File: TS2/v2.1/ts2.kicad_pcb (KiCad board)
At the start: 2 copper layers, 134.6 x 208.3 mm, 110 parts, among them P1 FTDI (TERMINAL), P2 FTDI (HOST), P3 +5V POWER, SW1 RESET, SW2 SINGLE STEP/RUN, SW3 STEP, SW4 ABORT, SW5 POWER, U1 555, U10 74LS32, U11 HM6264, U12 28C64, U13 HM6264, U14 28C64, U15 HM6264, U16 28C64, U17 HM6264, U18 28C64, U19 74LS20, U2 8 MHz, U20 74LS74, U21 74LS161, U22 74LS161, U23 74LS74, U24 74LS260, U25 74LS260, U26 74LS138, U27 74LS138, U28 74LS148, U29 6850, U3 74LS00, U30 6850, U31 74HC4060, U32 74LS138, U33 74LS138, U34 74LS00, U35 74LS74, U36 74LS27, U37 74LS00, U4 74LS06, U5 74LS04, U6 68000, U7 74LS08, U8 74LS32, U9 74LS32, Y1 2.4576MHz

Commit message: Rev 2.1.1 changes.
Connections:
- P3 pad 2: Net-(P3-Pad2) -> POWER
- SW5 pad 1: Net-(P3-Pad2) -> POWER
- U29 pad 1: (no net) -> GND
- U29 pad 12: (no net) -> VCC
- U30 pad 1: (no net) -> GND
- U30 pad 12: (no net) -> VCC
- U6 pad 7: LDS* -> UDS*
- U6 pad 8: UDS* -> LDS*
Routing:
- net UDS*: track 265.0 -> 561.0 mm, vias 5 -> 9
- net POWER: track 38.1 -> 277.3 mm, vias 0 -> 1
- net Net-(P3-Pad2): track 202.7 -> 0.00 mm
- net LDS*: track 274.4 -> 224.2 mm, vias 5 -> 6
- net VCC: track 1108.4 -> 1139.0 mm, vias 1 -> 2
- net GND: track 1388.1 -> 1408.3 mm, vias 1 -> 2
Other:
- board text added: "TS2 Single Board Computer Rev 2.1.1 Copyright (c) 2017 Jeff Tranter <tranter@pobox.com>"
- board text removed: "TS2 Single Board Computer Rev 2.1 Copyright (c) 2017 Jeff Tranter <tranter@pobox.com>"

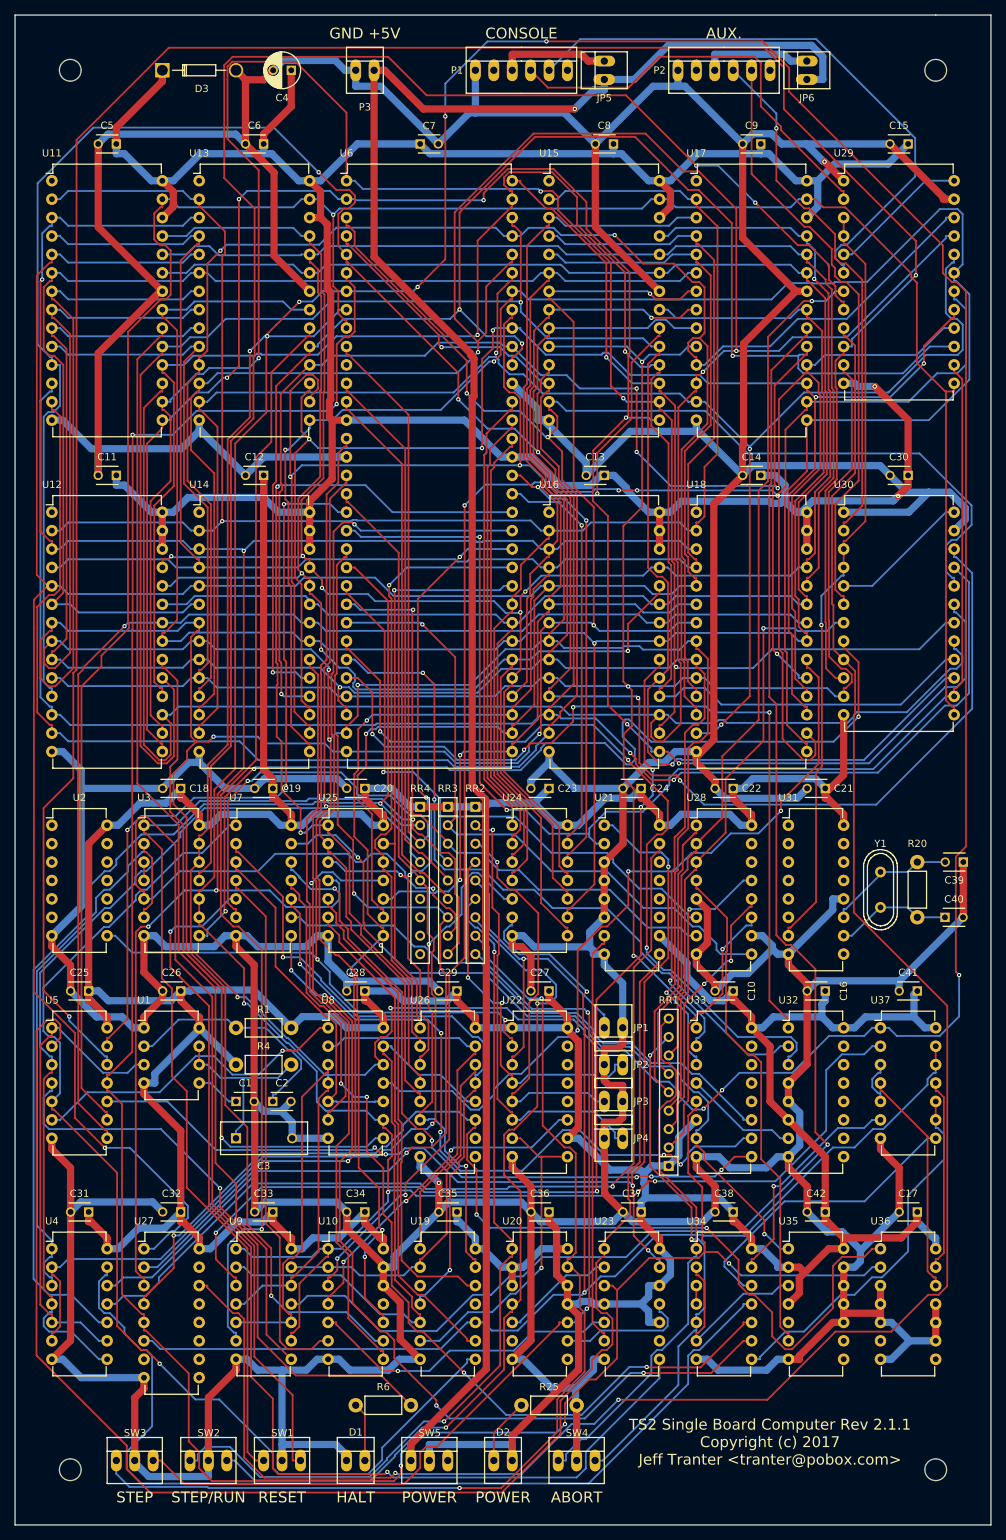
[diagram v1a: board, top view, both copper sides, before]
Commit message: Check in rev 2.1.1 PCB layout.
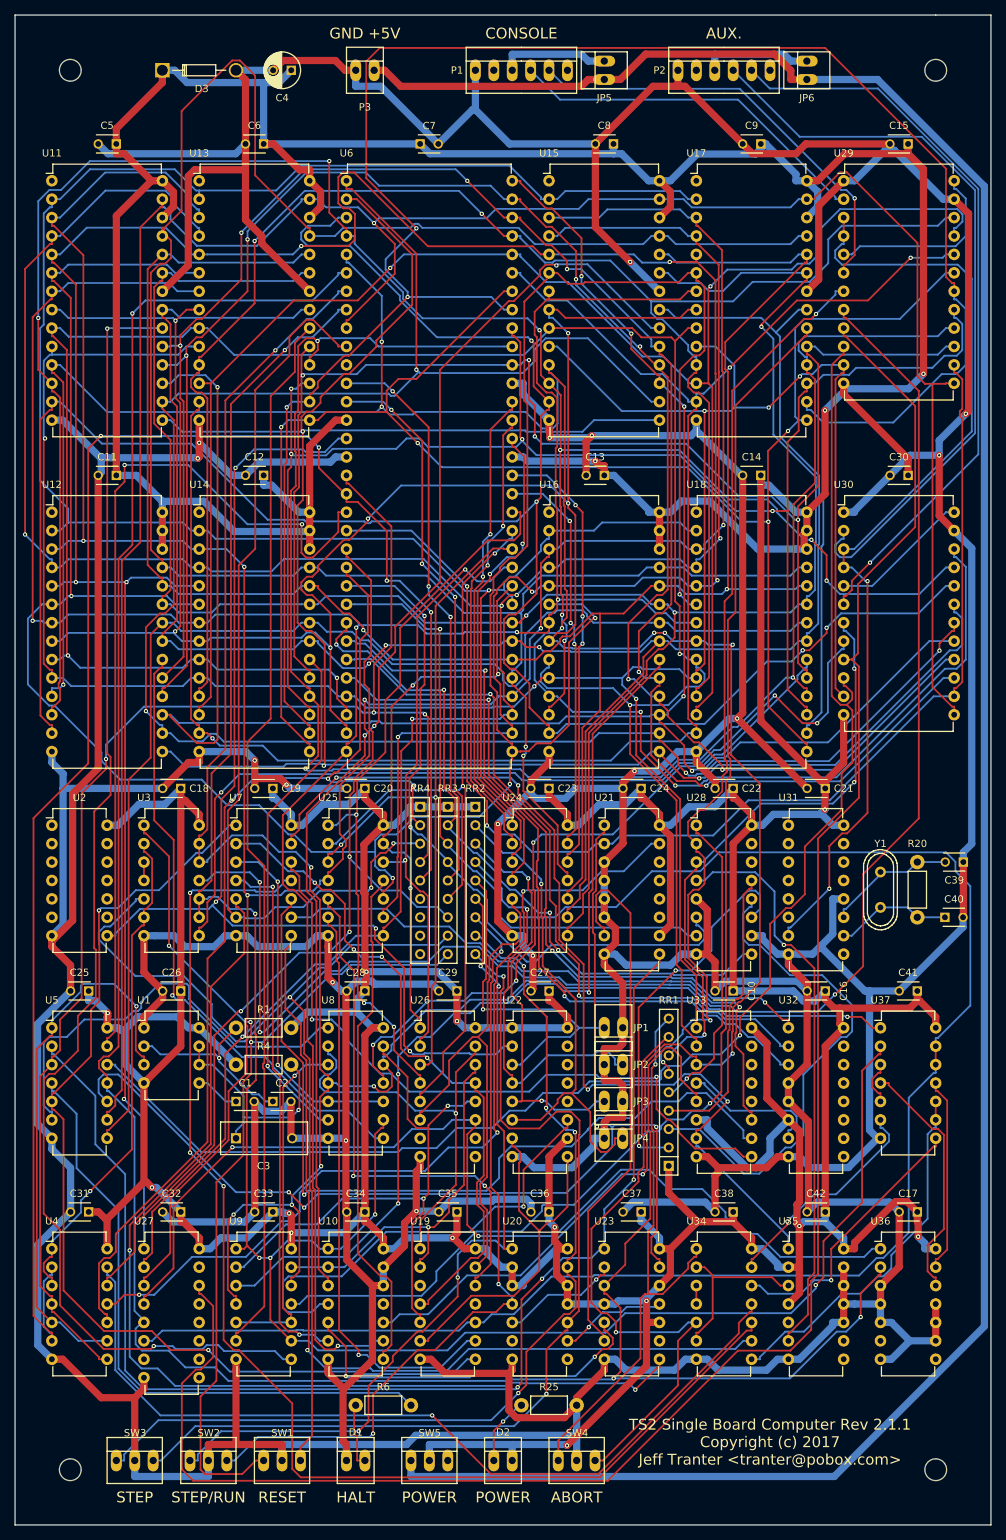
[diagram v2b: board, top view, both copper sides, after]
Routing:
- net UDS*: track 561.0 -> 281.9 mm, vias 9 -> 7
- net GND: track 1408.3 -> 1571.2 mm, vias 2 -> 16
- net Net-(U29-Pad10): track 336.8 -> 208.7 mm, vias 2 -> 1
- net VCC: track 1139.0 -> 1254.9 mm, vias 2 -> 16
- net LDS*: track 224.2 -> 312.9 mm
- net A05: track 291.8 -> 372.6 mm, vias 2 -> 5
- net RESET*: track 164.6 -> 240.9 mm, vias 1 -> 4
- net D12: track 243.5 -> 311.4 mm, vias 5 -> 3
- net POWER: track 277.3 -> 342.4 mm, vias 1 -> 0
- net D15: track 255.2 -> 201.5 mm, vias 5 -> 4
- net Net-(U34-Pad10): track 127.3 -> 174.1 mm, vias 4 -> 3
- net D09: track 283.9 -> 237.4 mm, vias 3 -> 2
- net Net-(U19-Pad10): track 190.5 -> 233.0 mm, vias 2 -> 0
- net A09: track 279.4 -> 317.9 mm, vias 6 -> 2
- net A04: track 387.7 -> 349.6 mm
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
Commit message: add updated gerber & drill files
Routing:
- added copper zone on B.Cu, net GND
- added copper zone on F.Cu, net GND
